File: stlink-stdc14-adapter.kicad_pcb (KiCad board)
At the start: 2 copper layers, 25.4 x 38.1 mm, 3 parts, among them J1 Conn_ST_STDC14, J2 Conn_ARM_JTAG_SWD_20, J3 Conn_01x04

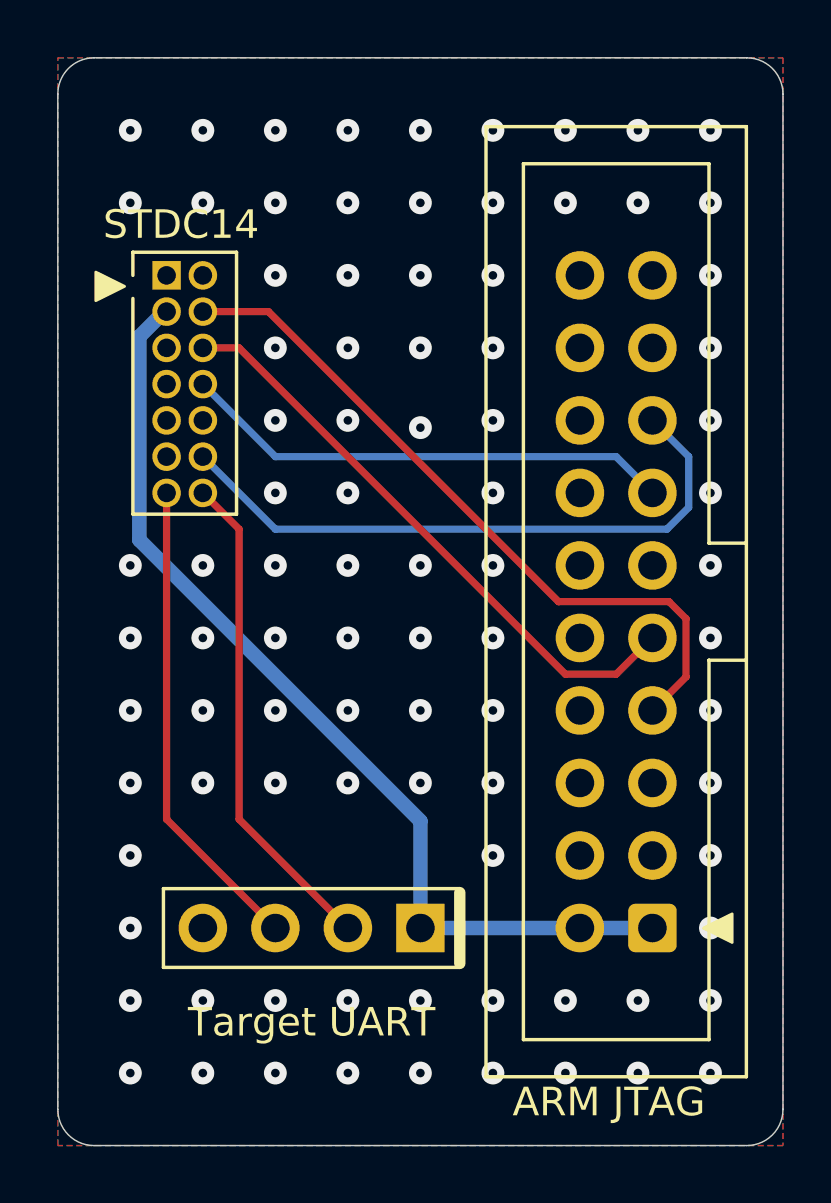
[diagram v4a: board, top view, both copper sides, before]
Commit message: add mounting holes, move UART slightly farther from JTAG
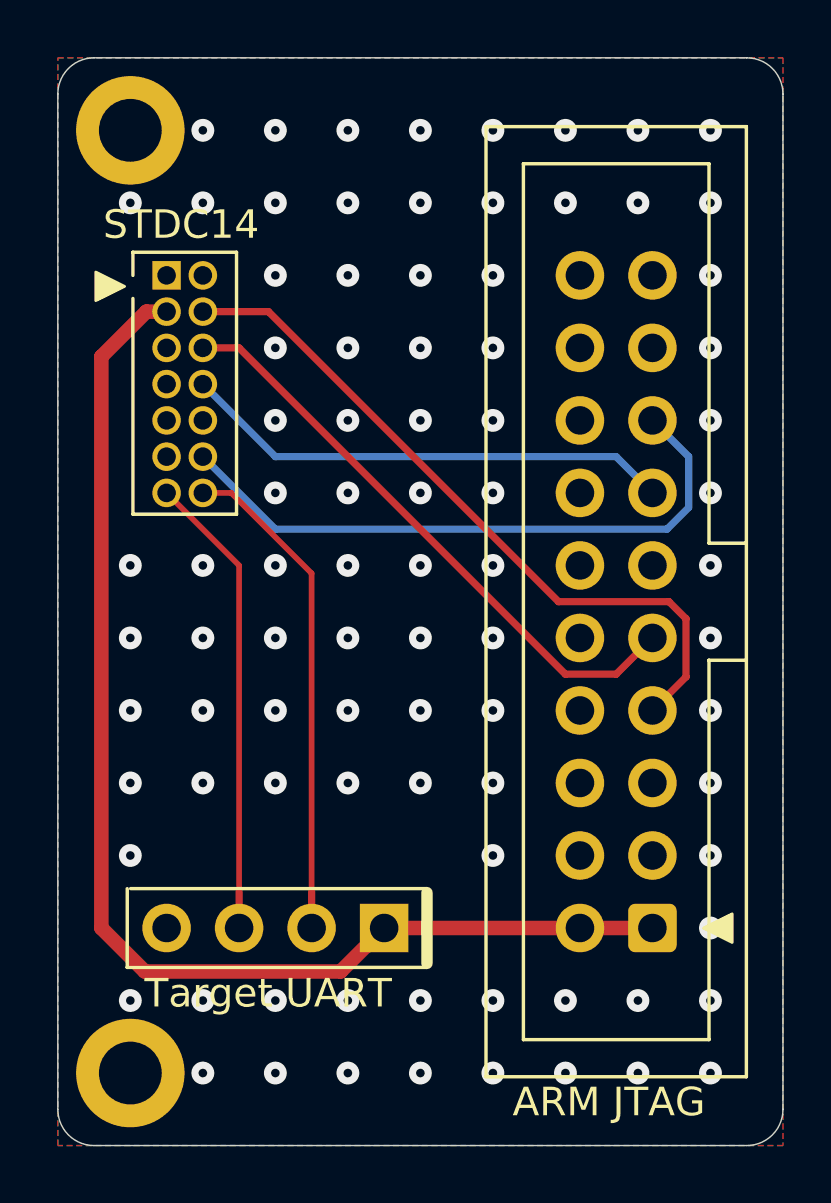
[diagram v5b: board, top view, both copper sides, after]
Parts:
- added REF**: MountingHole_2.2mm_M2_ISO14580_Pad, MountingHole:MountingHole_2.2mm_M2_ISO14580_Pad, F.Cu at (116.8, 111.8)
- added REF**: MountingHole_2.2mm_M2_ISO14580_Pad, MountingHole:MountingHole_2.2mm_M2_ISO14580_Pad, F.Cu at (116.8, 78.7)
- moved J3 1.27 mm to (125.7, 106.7)
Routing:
- net VCC: track 34.2 -> 43.6 mm
- net /UART_RX: track 16.8 -> 16.3 mm
- net GND: vias 88 -> 86
